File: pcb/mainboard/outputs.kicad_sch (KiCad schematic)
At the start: 71 parts, among them U38 ISL24021IRT065Z-T7A‎, U39 ISL24021IRT065Z-T7A‎, U40 ISL24021IRT065Z-T7A‎, U41 ISL24021IRT065Z-T7A‎, U42 DAC60508, U43 ISL24021IRT065Z-T7A‎, U44 ISL24021IRT065Z-T7A‎, U45 ISL24021IRT065Z-T7A‎, U46 ISL24021IRT065Z-T7A‎, U47 74LVC1T45, U48 74LVC1T45, U49 74LVC1T45, U50 74LVC1T45, U51 74LVC1T45, U52 74LVC1T45, U53 74LVC1T45, U54 74LVC1T45, U8 XC7K70T-2FBG484C

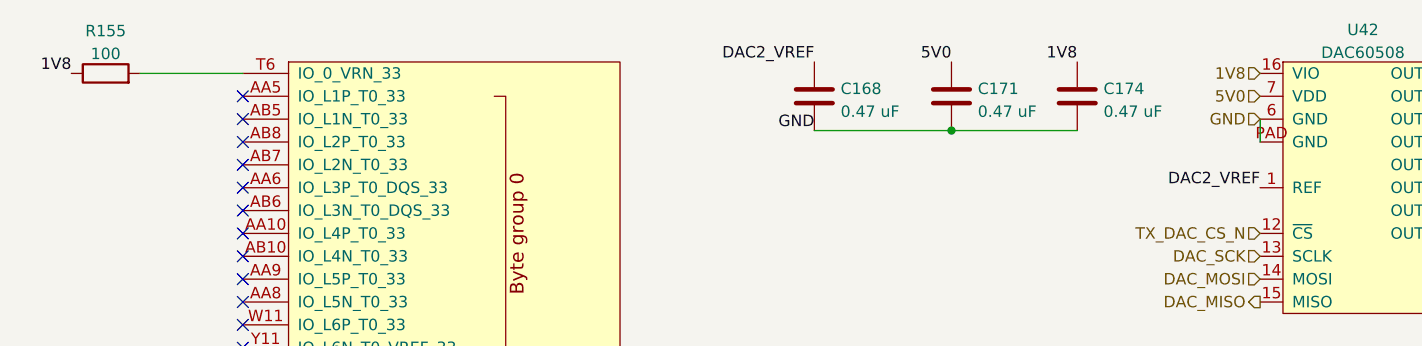
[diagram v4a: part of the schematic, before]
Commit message: Finished initial schematic review of trigger crossbar mainboard
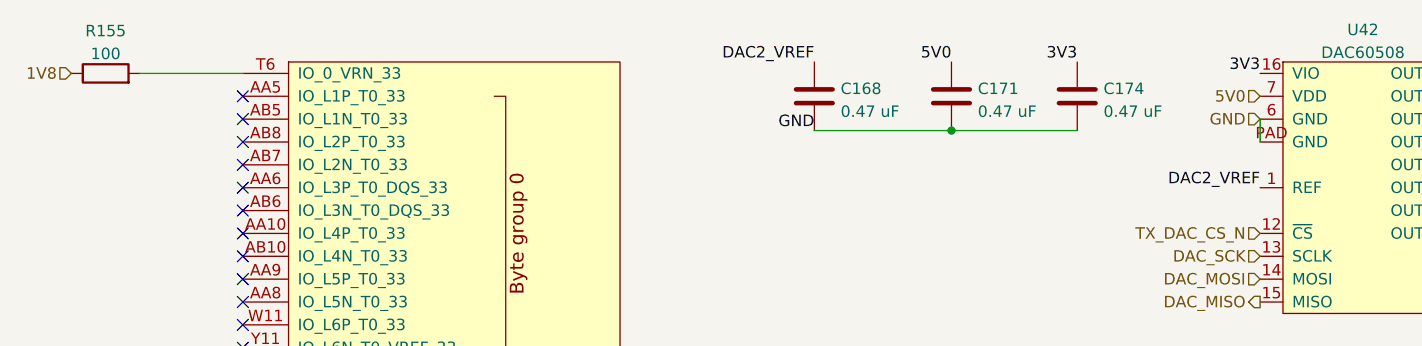
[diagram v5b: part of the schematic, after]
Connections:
- net 1V8: no longer C174.1, U42.16 (VIO)
- net 3V3: now also C174.1, U42.16 (VIO)
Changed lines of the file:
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@@
   (title_block
     (title "Trigger Crossbar")
-    (date "2023-12-18")
+    (date "2023-12-19")
     (rev "0.1")
     (company "Antikernel Labs")
@@
     (effects (font (size 1.27 1.27)) (justify right bottom))
   )
-  (label "1V8" (at 50.8 26.67 180)
-    (effects (font (size 1.27 1.27)) (justify right bottom))
-  )
   (label "GND" (at 173.99 121.92 180)
     (effects (font (size 1.27 1.27)) (justify right bottom))
@@
     (effects (font (size 1.27 1.27)) (justify right bottom))
   )
-  (label "1V8" (at 162.56 25.4 180)
+  (label "3V3" (at 162.56 25.4 180)
     (effects (font (size 1.27 1.27)) (justify right bottom))
   )
@@
   (label "VCCIO_7" (at 156.21 114.3 0)
     (effects (font (size 1.27 1.27)) (justify left bottom))
+  )
+  (label "3V3" (at 182.88 26.67 180)
+    (effects (font (size 1.27 1.27)) (justify right bottom))
   )
   (label "VREF_OUT5" (at 72.39 229.87 180)
@@
     (effects (font (size 1.27 1.27)) (justify right))
   )
+  (hierarchical_label "1V8" (shape input) (at 50.8 26.67 180)
+    (effects (font (size 1.27 1.27)) (justify right))
+  )
   (hierarchical_label "OUT4" (shape output) (at 156.21 72.39 0)
     (effects (font (size 1.27 1.27)) (justify left))
@@
     (effects (font (size 1.27 1.27)) (justify right))
   )
-  (hierarchical_label "1V8" (shape input) (at 182.88 26.67 180)
-    (effects (font (size 1.27 1.27)) (justify right))
-  )

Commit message: Initial FPGA routing
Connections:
- net OE10A: now also U8.T20 (IO_L6P_T0_13); no longer U8.E14 (IO_L6P_T0_15)
- net OE10B: now also U8.AA20 (IO_L8P_T1_13); no longer U8.B16 (IO_L8P_T1_AD3P_15)
- net OE11A: now also U8.U20 (IO_L6N_T0_VREF_13); no longer U8.D14 (IO_L6N_T0_VREF_15)
- net OE11B: now also U8.AB21 (IO_L8N_T1_13); no longer U8.A16 (IO_L8N_T1_AD3N_15)
- net OE8A: now also U8.U17 (IO_L5P_T0_13); no longer U8.C13 (IO_L5P_T0_AD2P_15)
- net OE8B: now also U8.Y21 (IO_L7P_T1_13); no longer U8.C14 (IO_L7P_T1_AD10P_15)
- net OE9A: now also U8.V18 (IO_L5N_T0_13); no longer U8.B13 (IO_L5N_T0_AD2N_15)
- net OE9B: now also U8.Y22 (IO_L7N_T1_13); no longer U8.C15 (IO_L7N_T1_AD10N_15)
- net OUT0: now also U8.AA3 (IO_L23P_T3_34); no longer U8.V13 (IO_L23P_T3_33)
- net OUT1: now also U8.AB2 (IO_L23N_T3_34); no longer U8.V12 (IO_L23N_T3_33)
- net OUT10_3V3: now also U8.W21 (IO_L4P_T0_13); no longer U8.A13 (IO_L4P_T0_AD9P_15)
- net OUT11_3V3: now also U8.W22 (IO_L4N_T0_13); no longer U8.A14 (IO_L4N_T0_AD9N_15)
- net OUT2: now also U8.AA4 (IO_L24P_T3_34); no longer U8.T13 (IO_L24P_T3_33)
- net OUT3: now also U8.AB3 (IO_L24N_T3_34); no longer U8.U13 (IO_L24N_T3_33)
- net OUT4_3V3: now also U8.T21 (IO_L1P_T0_13); no longer U8.G15 (IO_L1P_T0_AD0P_15)
- net OUT5_3V3: now also U8.U21 (IO_L1N_T0_13); no longer U8.G16 (IO_L1N_T0_AD0N_15)
- net OUT6_3V3: now also U8.U22 (IO_L2P_T0_13); no longer U8.C12 (IO_L2P_T0_AD8P_15)
- net OUT7_3V3: now also U8.V22 (IO_L2N_T0_13); no longer U8.B12 (IO_L2N_T0_AD8N_15)
- net OUT8_3V3: now also U8.T18 (IO_L3P_T0_DQS_13); no longer U8.F15 (IO_L3P_T0_DQS_AD1P_15)
- net OUT9_3V3: now also U8.U18 (IO_L3N_T0_DQS_13); no longer U8.F16 (IO_L3N_T0_DQS_AD1N_15)
- net at R156.2: now also U8.V5 (IO_25_VRP_34); no longer U8.T14 (IO_25_VRP_33)
- net at R155.2: now also U8.K4 (IO_0_VRN_34); no longer U8.T6 (IO_0_VRN_33)
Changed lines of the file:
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@@
   (title_block
     (title "Trigger Crossbar")
-    (date "2023-12-20")
+    (date "2023-12-22")
     (rev "0.1")
     (company "Antikernel Labs")
@@
     (pin "2")
   )
-  (symbol (lib_id "xilinx-azonenberg:XC7KxT-FBG484") (at 354.33 151.13 0) (unit 5)
+  (symbol (lib_id "xilinx-azonenberg:XC7KxT-FBG484") (at 354.33 151.13 0) (unit 3)
     (in_bom yes) (on_board yes)
     (property "Reference" "U8" (id 0) (at 355.6 154.94 0)
@@
     (pin "2")
   )
-  (symbol (lib_id "xilinx-azonenberg:XC7KxT-FBG484") (at 74.93 151.13 0) (unit 7)
+  (symbol (lib_id "xilinx-azonenberg:XC7KxT-FBG484") (at 74.93 151.13 0) (unit 8)
     (in_bom yes) (on_board yes)
     (property "Reference" "U8" (id 0) (at 76.2 154.94 0)

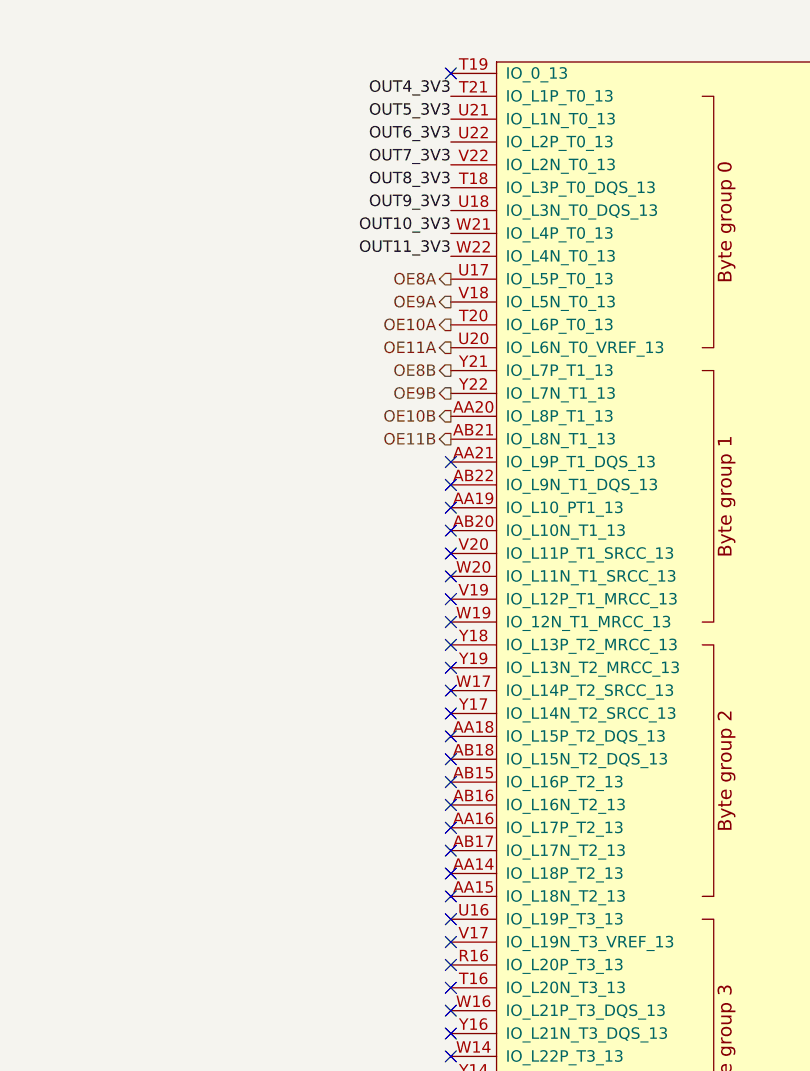
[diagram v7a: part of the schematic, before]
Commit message: Placed remainder of relays and drivers
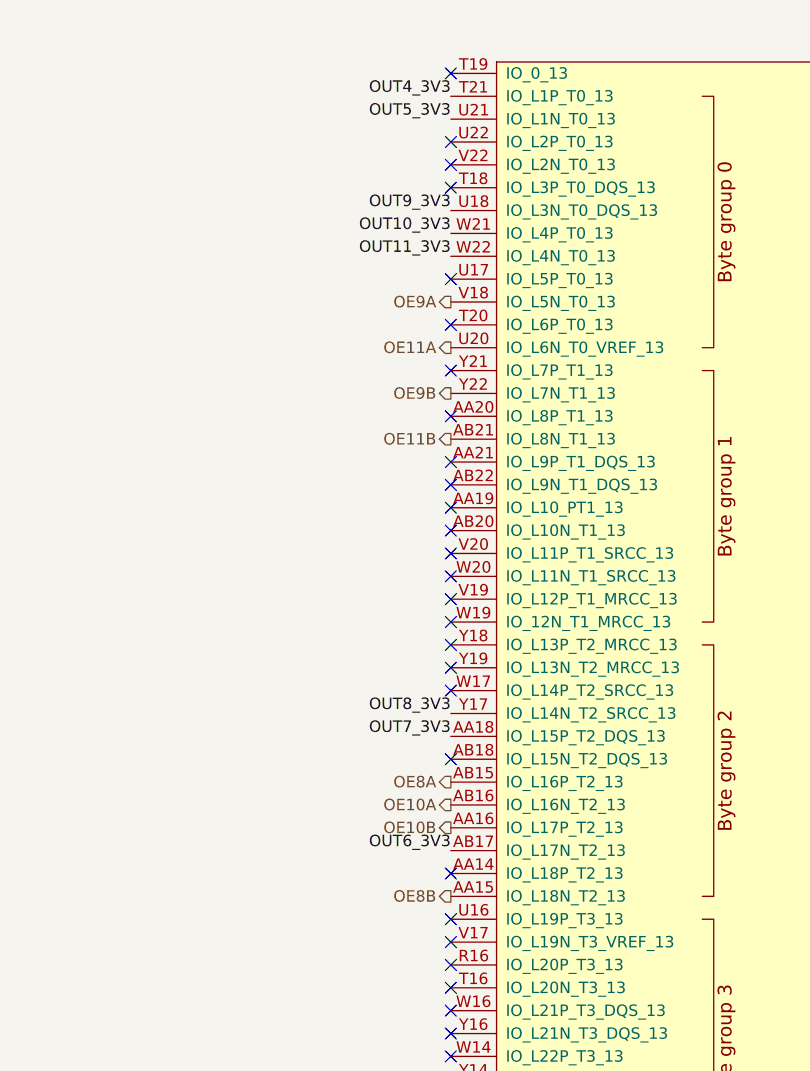
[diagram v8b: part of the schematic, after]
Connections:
- net OE10A: now also U8.AB16 (IO_L16N_T2_13); no longer U8.T20 (IO_L6P_T0_13)
- net OE10B: now also U8.AA16 (IO_L17P_T2_13); no longer U8.AA20 (IO_L8P_T1_13)
- net OE8A: now also U8.AB15 (IO_L16P_T2_13); no longer U8.U17 (IO_L5P_T0_13)
- net OE8B: now also U8.AA15 (IO_L18N_T2_13); no longer U8.Y21 (IO_L7P_T1_13)
- net OUT6_3V3: now also U8.AB17 (IO_L17N_T2_13); no longer U8.U22 (IO_L2P_T0_13)
- net OUT7_3V3: now also U8.AA18 (IO_L15P_T2_DQS_13); no longer U8.V22 (IO_L2N_T0_13)
- net OUT8_3V3: now also U8.Y17 (IO_L14N_T2_SRCC_13); no longer U8.T18 (IO_L3P_T0_DQS_13)
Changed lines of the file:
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@@
   (junction (at 204.47 210.82) (diameter 0) (color 0 0 0 0)
   )
-  (no_connect (at 349.25 100.33))
+  (no_connect (at 349.25 59.69))
   (no_connect (at 69.85 62.23))
   (no_connect (at 69.85 90.17))
+  (no_connect (at 349.25 36.83))
   (no_connect (at 349.25 138.43))
   (no_connect (at 69.85 74.93))
+  (no_connect (at 349.25 39.37))
   (no_connect (at 349.25 26.67))
   (no_connect (at 349.25 95.25))
@@
   (no_connect (at 69.85 135.89))
   (no_connect (at 69.85 128.27))
-  (no_connect (at 349.25 97.79))
   (no_connect (at 69.85 130.81))
   (no_connect (at 69.85 80.01))
@@
   (no_connect (at 349.25 74.93))
   (no_connect (at 349.25 102.87))
+  (no_connect (at 349.25 54.61))
   (no_connect (at 69.85 31.75))
-  (no_connect (at 349.25 110.49))
+  (no_connect (at 349.25 34.29))
   (no_connect (at 349.25 87.63))
   (no_connect (at 69.85 87.63))
@@
   (no_connect (at 69.85 120.65))
   (no_connect (at 69.85 118.11))
+  (no_connect (at 349.25 49.53))
   (no_connect (at 69.85 77.47))
   (no_connect (at 349.25 77.47))
@@
   (no_connect (at 69.85 138.43))
   (no_connect (at 69.85 59.69))
-  (no_connect (at 349.25 107.95))
   (no_connect (at 349.25 82.55))
   (no_connect (at 349.25 125.73))
@@
   (no_connect (at 69.85 41.91))
   (no_connect (at 69.85 46.99))
-  (no_connect (at 349.25 113.03))
   (no_connect (at 69.85 36.83))
   (no_connect (at 69.85 82.55))
@@
   (no_connect (at 69.85 64.77))
   (no_connect (at 349.25 128.27))
-  (no_connect (at 349.25 105.41))
   (no_connect (at 349.25 130.81))
   (no_connect (at 69.85 95.25))
@@
   (no_connect (at 69.85 102.87))
   (no_connect (at 69.85 29.21))
-  (no_connect (at 349.25 118.11))
   (no_connect (at 349.25 85.09))
   (no_connect (at 349.25 115.57))
@@
   (no_connect (at 349.25 146.05))
   (no_connect (at 69.85 110.49))
+  (no_connect (at 349.25 64.77))
   (no_connect (at 349.25 120.65))
   (no_connect (at 69.85 105.41))
@@
     (effects (font (size 1.27 1.27)) (justify right bottom))
   )
-  (label "OUT7_3V3" (at 349.25 36.83 180)
+  (label "OUT7_3V3" (at 349.25 100.33 180)
     (effects (font (size 1.27 1.27)) (justify right bottom))
   )
@@
     (effects (font (size 1.27 1.27)) (justify left bottom))
   )
-  (label "OUT8_3V3" (at 349.25 39.37 180)
+  (label "OUT8_3V3" (at 349.25 97.79 180)
     (effects (font (size 1.27 1.27)) (justify right bottom))
   )
@@
     (effects (font (size 1.27 1.27)) (justify left bottom))
   )
-  (label "OUT6_3V3" (at 349.25 34.29 180)
+  (label "OUT6_3V3" (at 349.25 113.03 180)
     (effects (font (size 1.27 1.27)) (justify right bottom))
   )
@@
     (effects (font (size 1.27 1.27)) (justify right))
   )
-  (hierarchical_label "OE8A" (shape output) (at 349.25 49.53 180)
+  (hierarchical_label "OE8A" (shape output) (at 349.25 105.41 180)
     (effects (font (size 1.27 1.27)) (justify right))
   )
@@
     (effects (font (size 1.27 1.27)) (justify right))
   )
-  (hierarchical_label "OE8B" (shape output) (at 349.25 59.69 180)
+  (hierarchical_label "OE8B" (shape output) (at 349.25 118.11 180)
     (effects (font (size 1.27 1.27)) (justify right))
   )
@@
     (effects (font (size 1.27 1.27)) (justify right))
   )
-  (hierarchical_label "OE10B" (shape output) (at 349.25 64.77 180)
+  (hierarchical_label "OE10B" (shape output) (at 349.25 110.49 180)
     (effects (font (size 1.27 1.27)) (justify right))
   )
@@
     (effects (font (size 1.27 1.27)) (justify right))
   )
-  (hierarchical_label "OE10A" (shape output) (at 349.25 54.61 180)
-    (effects (font (size 1.27 1.27)) (justify right))
-  )
+  (hierarchical_label "OE10A" (shape output) (at 349.25 107.95 180)
+    (effects (font (size 1.27 1.27)) (justify right))
+  )
